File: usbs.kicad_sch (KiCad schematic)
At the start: 14 parts, among them J13 0473460001, J15 0473460001, J4 USB-A_Amphenol_UE27AC54100, U4 FT234XD-R

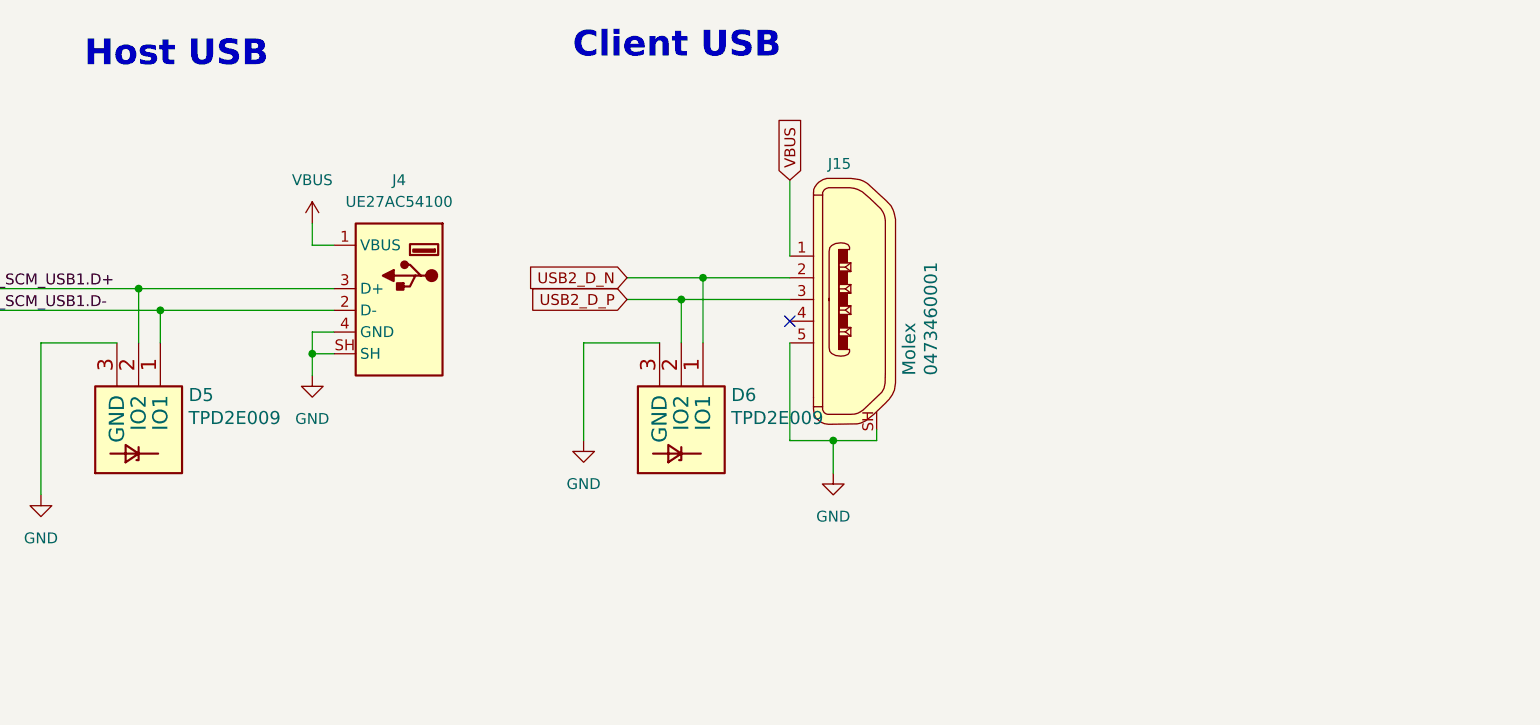
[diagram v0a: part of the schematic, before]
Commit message: [#92504] Clear Wire BUS errors
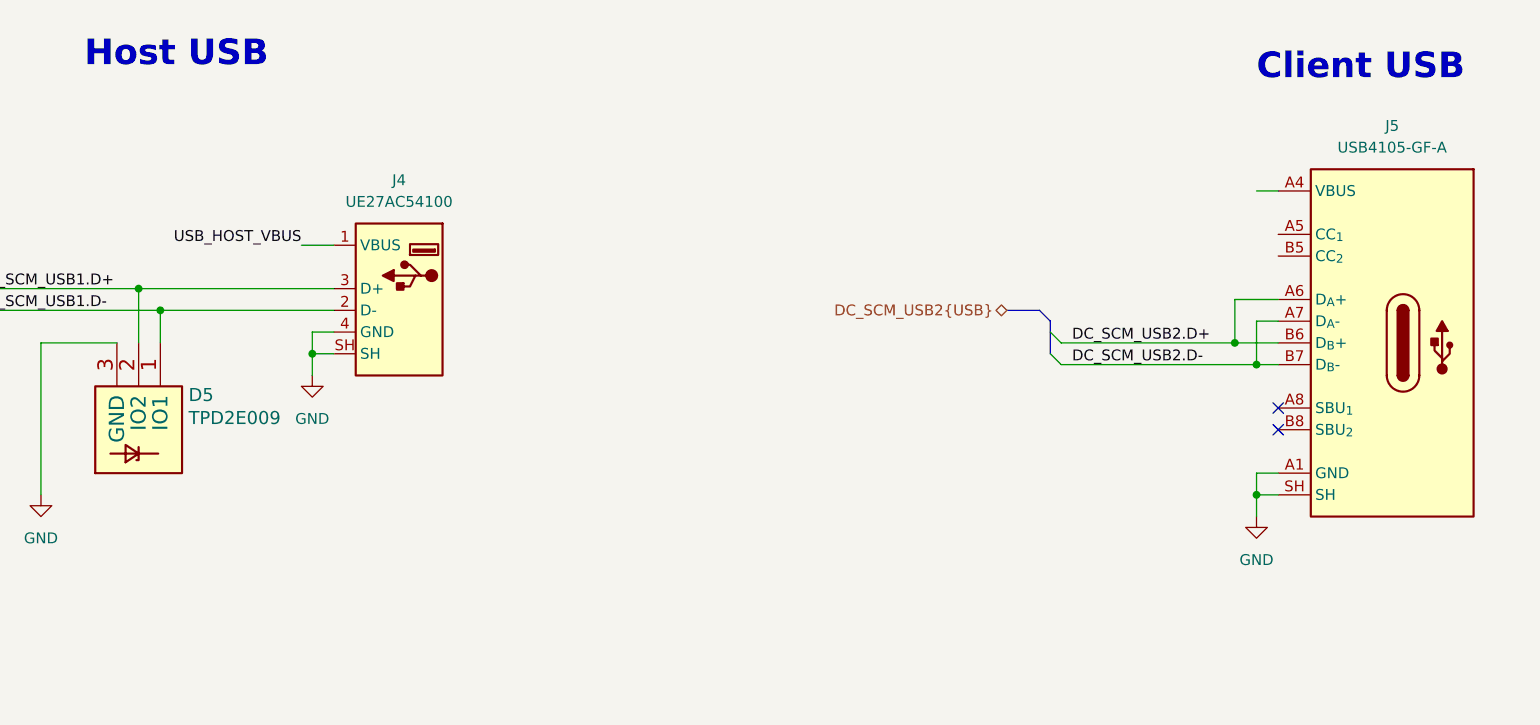
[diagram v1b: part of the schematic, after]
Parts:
- removed D6: TPD2E009, bmc-breakout-board-footprints:SOT-3, symbol bmc-breakout-board:TPD2E009
- removed J15: 0473460001, bmc-breakout-board-footprints:USB_Micro_B_Female_0473460001, symbol bmc-breakout-board:0473460001
- added J5: USB-C_GCT_USB4105-GF-A, antmicro-footprints:USB-C_Receptacle_GCT_USB4105-GF-A, symbol antmicroUSBConnectors:USB-C_GCT_USB4105-GF-A
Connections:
- net GND: now also J5.A1 (GND), J5.A12 (GND), J5.B1 (GND), J5.B12 (GND), J5.SH
- net VBUS: no longer J4.1 (VBUS)
- new net: J5.A4 (VBUS), J5.A9 (VBUS), J5.B4 (VBUS), J5.B9 (VBUS)
- new net DC_SCM_USB2.D+: J5.A6 (D_{A}+), J5.B6 (D_{B}+)
- new net DC_SCM_USB2.D-: J5.A7 (D_{A}-), J5.B7 (D_{B}-)
- new net USB_HOST_VBUS: J4.1 (VBUS)
- no-connect marks 3 -> 4

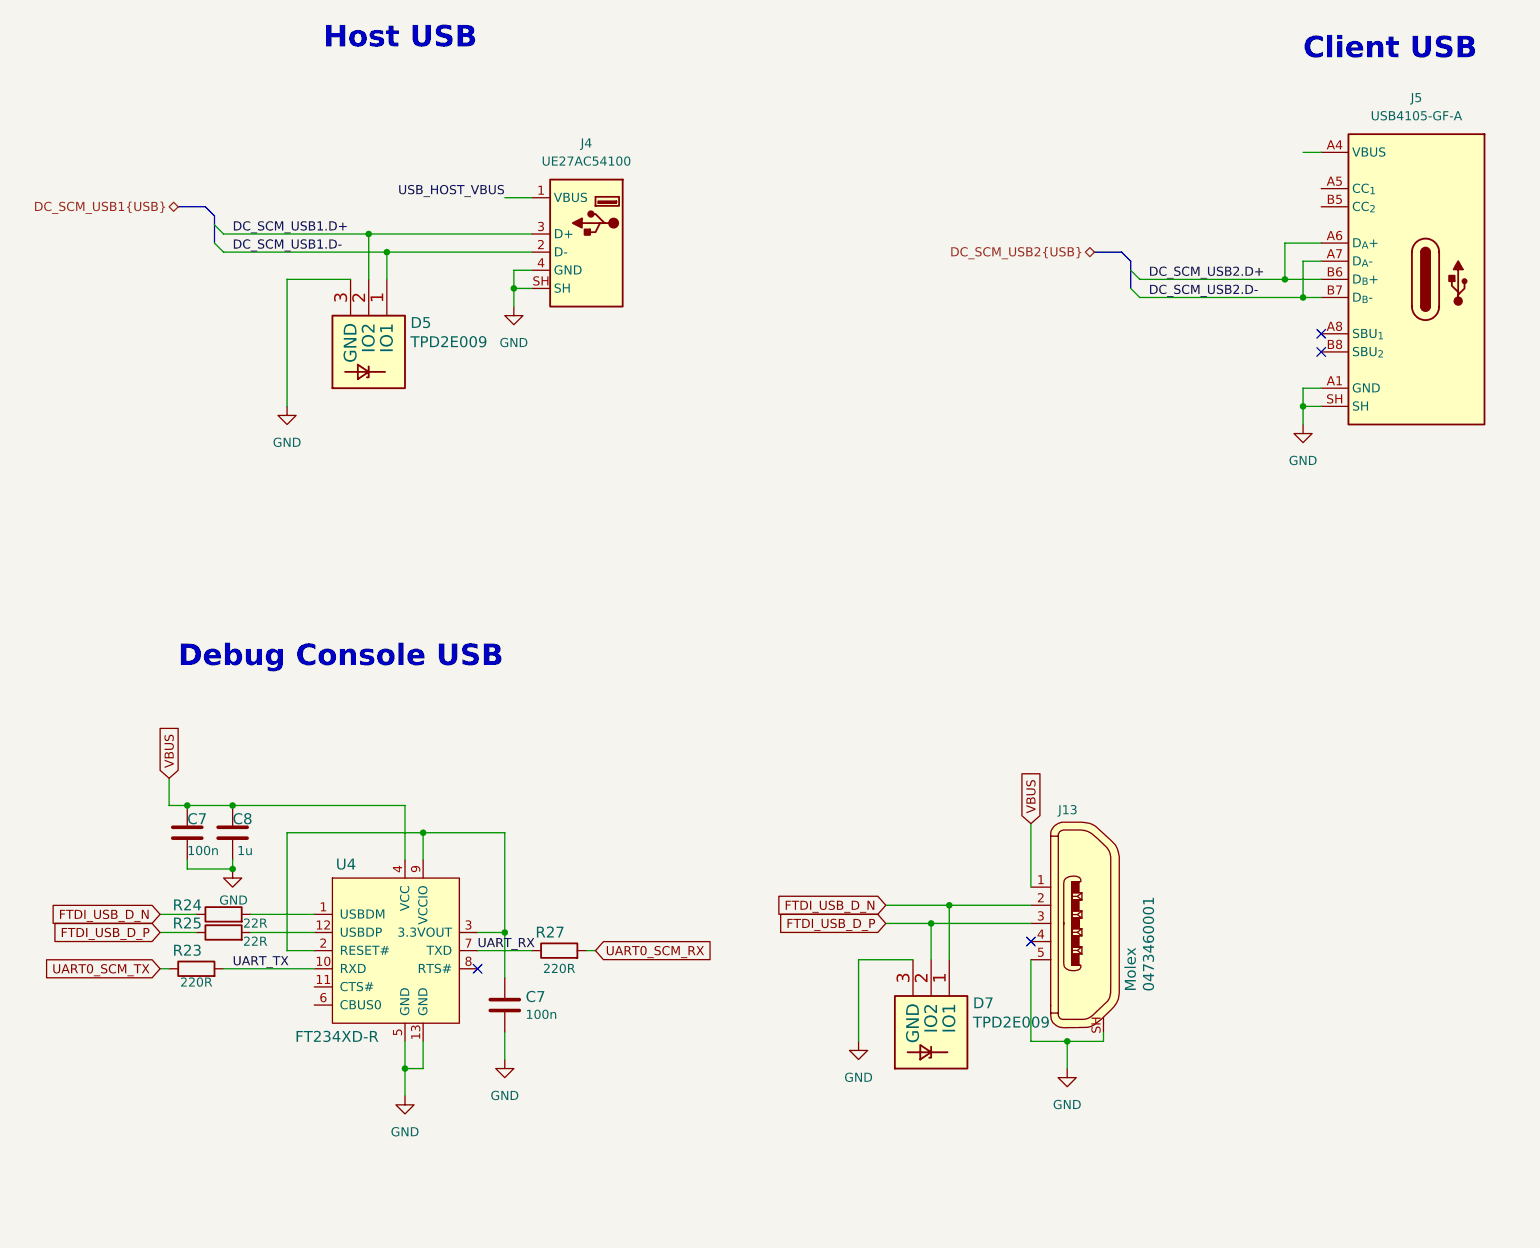
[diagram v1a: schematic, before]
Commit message: [#92504] Add Client USB
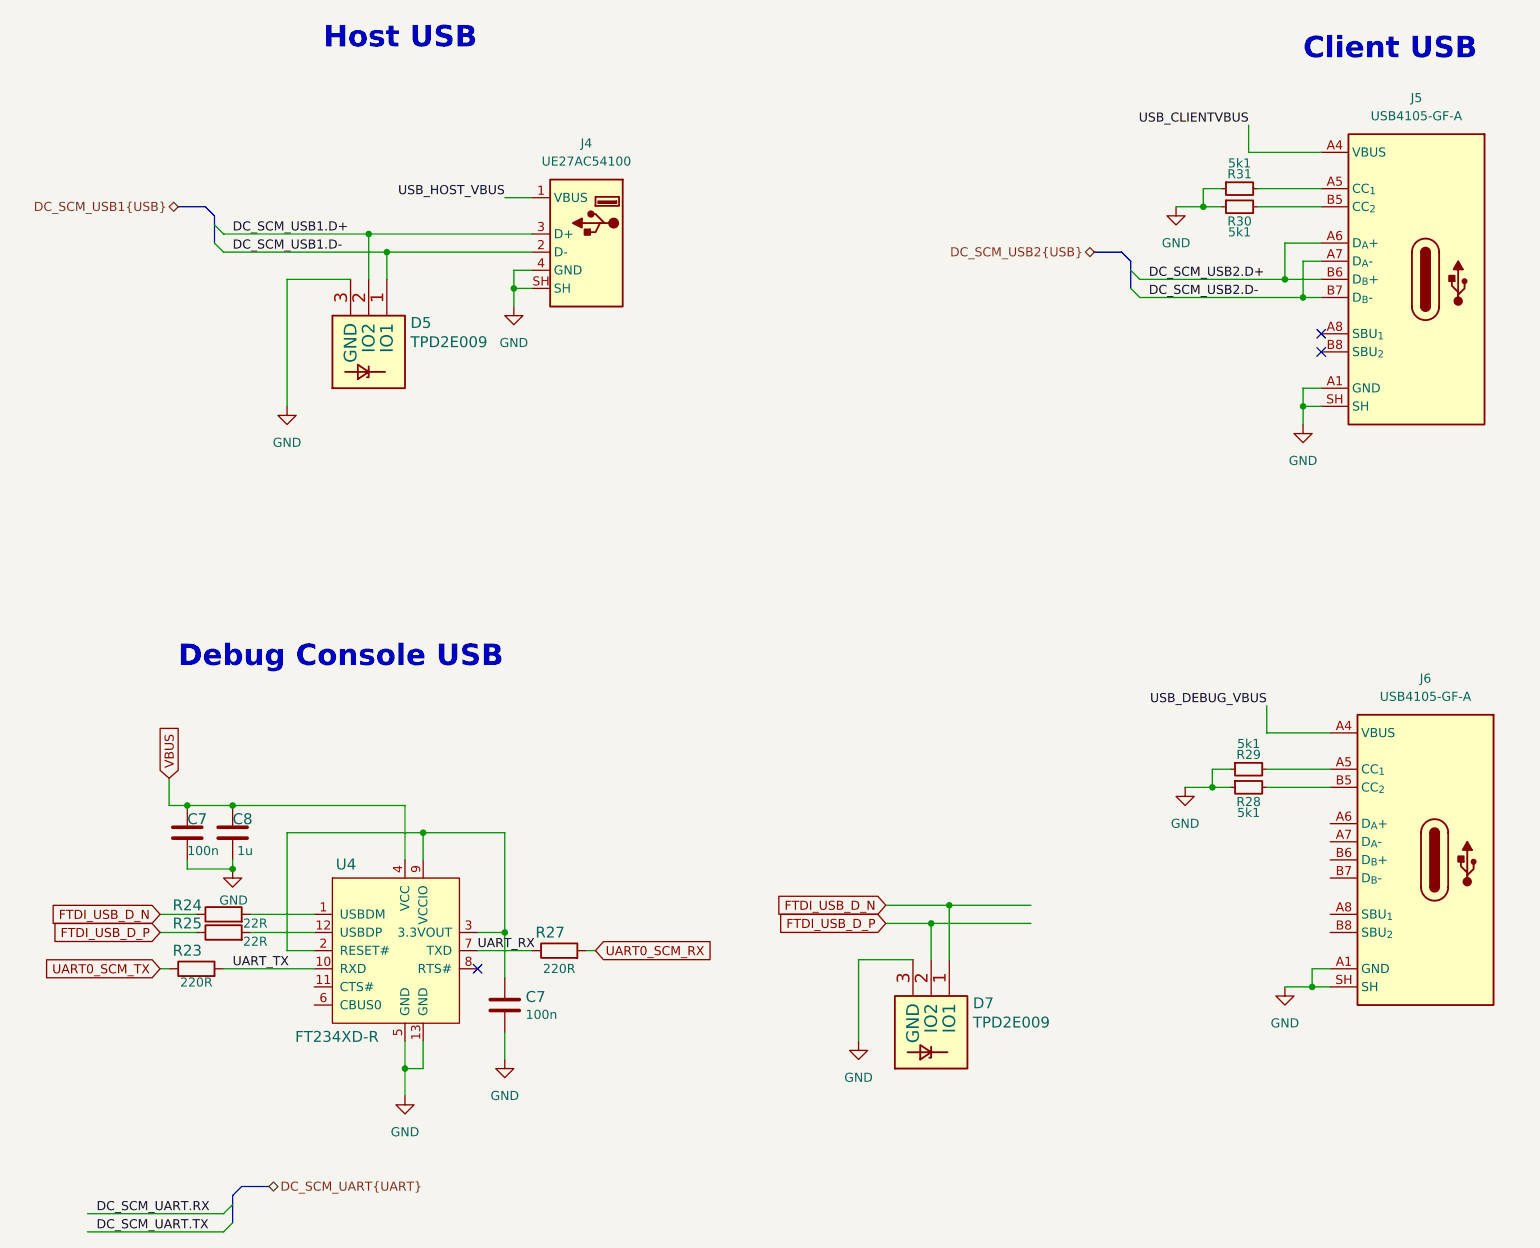
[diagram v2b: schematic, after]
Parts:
- removed J13: 0473460001, bmc-breakout-board-footprints:USB_Micro_B_Female_0473460001, symbol bmc-breakout-board:0473460001
- added J6: USB-C_GCT_USB4105-GF-A, antmicro-footprints:USB-C_Receptacle_GCT_USB4105-GF-A, symbol antmicroUSBConnectors:USB-C_GCT_USB4105-GF-A
- added R28, R29, R30, R31: R_5k1_0402, antmicro-footprints:R_0402_1005Metric, symbol antmicroResistors0402:R_5k1_0402
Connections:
- net GND: now also J6.A1 (GND), J6.A12 (GND), J6.B1 (GND), J6.B12 (GND), J6.SH, R28.1, R29.1, R30.1, R31.1
- net USB_CLIENTVBUS: now reaches J5.A4 (VBUS), J5.A9 (VBUS), J5.B4 (VBUS), J5.B9 (VBUS)
- net at J5.A5 (CC_{1}): now also R30.2
- net at J5.B5 (CC_{2}): now also R31.2
- new net: J6.A5 (CC_{1}), R28.2
- new net: J6.B5 (CC_{2}), R29.2
- new net USB_DEBUG_VBUS: J6.A4 (VBUS), J6.A9 (VBUS), J6.B4 (VBUS), J6.B9 (VBUS)
- no-connect marks 4 -> 3
